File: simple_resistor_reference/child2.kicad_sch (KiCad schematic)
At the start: 1 part

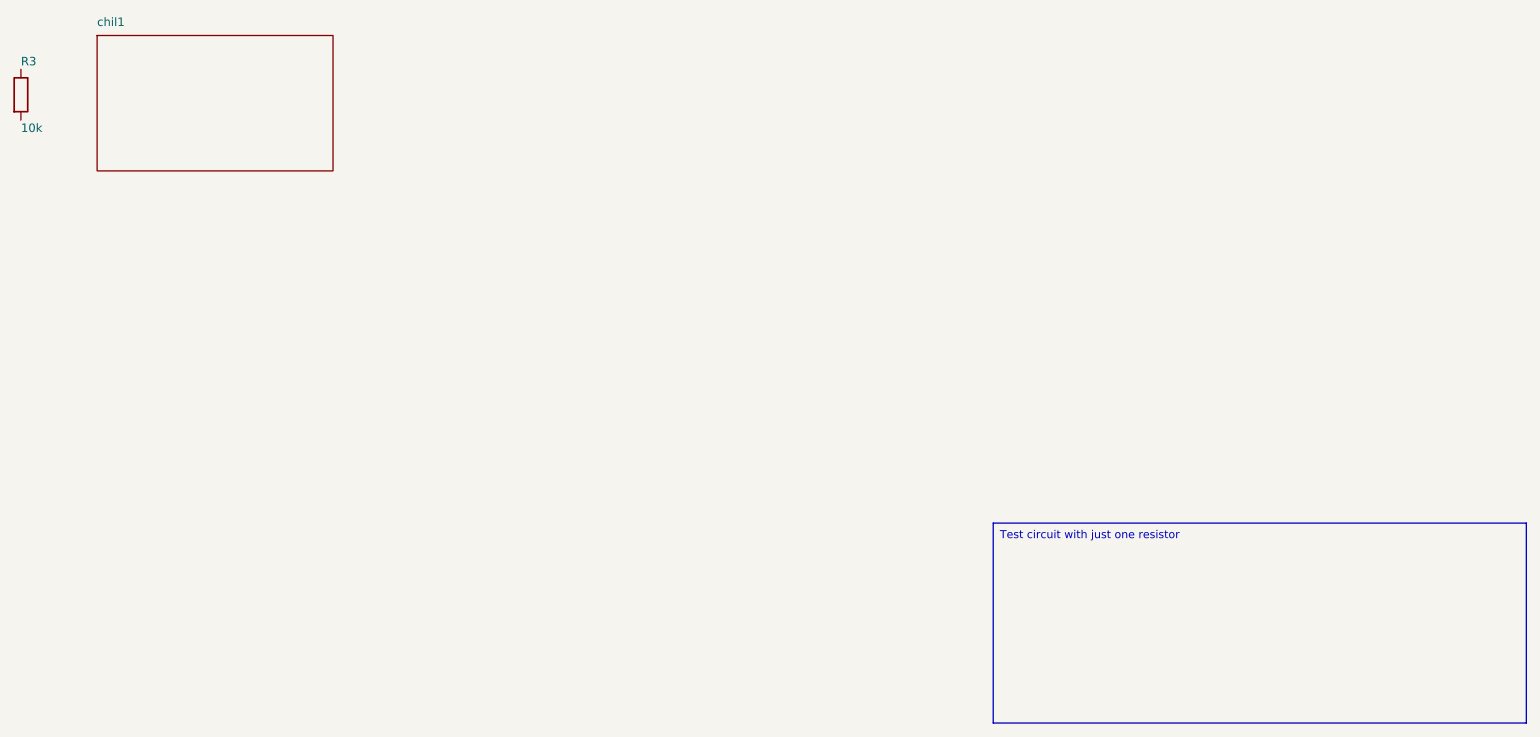
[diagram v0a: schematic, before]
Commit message: adding updated testing code
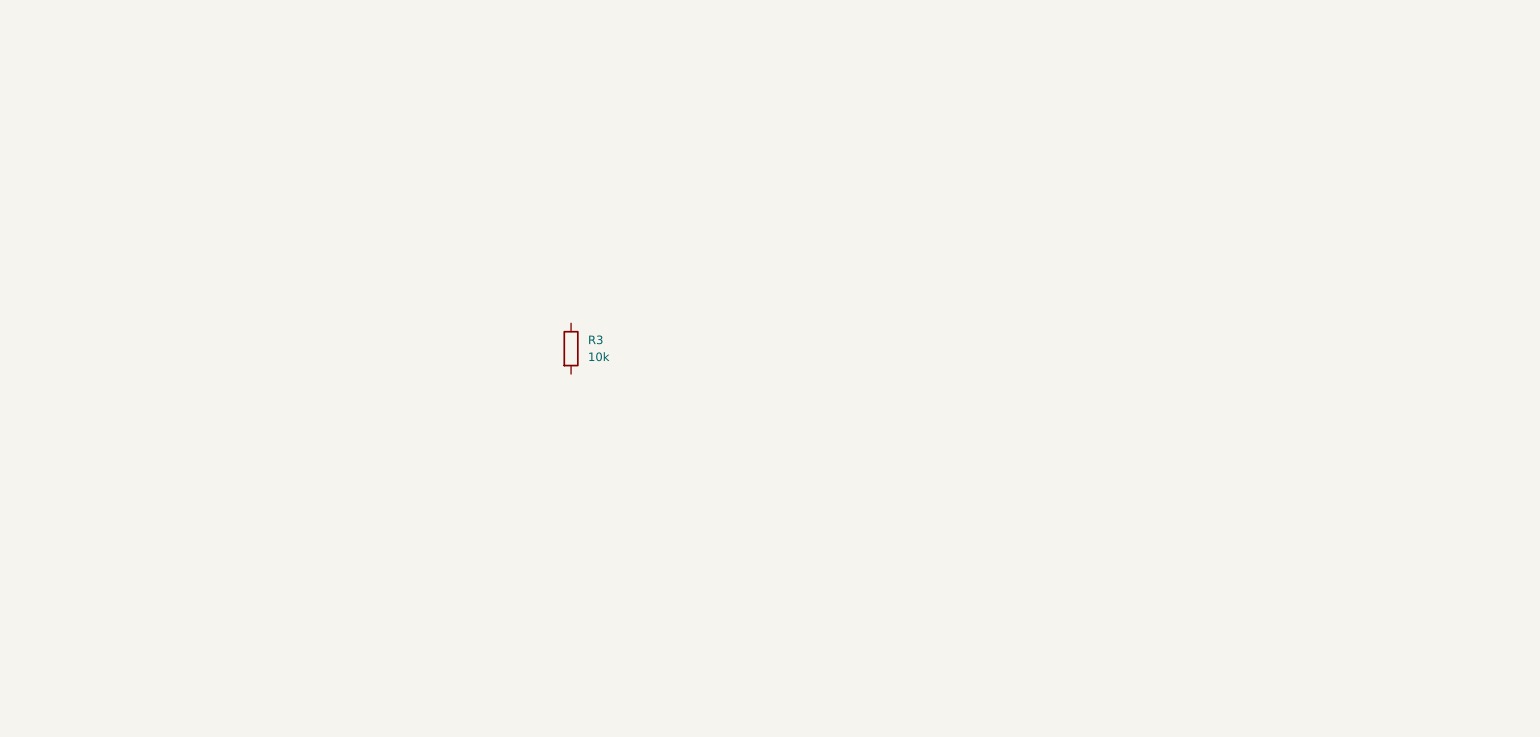
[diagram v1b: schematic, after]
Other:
- removed sheet chil1
- company: Circuit-Synth -> (none)
- title: singe_resistor_generated -> (none)
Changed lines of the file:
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@@
 (kicad_sch
 	(version 20250114)
-	(generator "kicad_api")
+	(generator "eeschema")
 	(generator_version "9.0")
 	(paper "A4")
-	(title_block
-		(title singe_resistor_generated)
-		(date 2025-08-04)
-		(company Circuit-Synth)
-	)
 	(symbol
 		(lib_id "Device:R")
-		(at 38.1 45.72 0)
+		(at 120.65 83.82 0)
 		(unit 1)
 		(exclude_from_sim no)
@@
 		(fields_autoplaced yes)
 		(property "Reference" "R3"
-			(at 38.1 40.72 0)
+			(at 123.19 82.5499 0)
 			(effects
 				(font
@@
 		)
 		(property "Value" "10k"
-			(at 38.1 50.72 0)
+			(at 123.19 85.0899 0)
 			(effects
 				(font
@@
 		)
 		(property "Footprint" "Resistor_SMD:R_0603_1608Metric"
-			(at 38.1 55.72 0)
+			(at 118.872 83.82 90)
 			(effects
 				(font
@@
 			)
 		)
+		(property "Datasheet" "~"
+			(at 120.65 83.82 0)
+			(effects
+				(font
+					(size 1.27 1.27)
+				)
+				(hide yes)
+			)
+		)
+		(property "Description" "Resistor"
+			(at 120.65 83.82 0)
+			(effects
+				(font
+					(size 1.27 1.27)
+				)
+				(hide yes)
+			)
+		)
+		(pin "2"
+		)
+		(pin "1"
+		)
 		(instances
-			(project
-				""
-				(path
-					"/4230698c-b526-4307-9655-afb80e239726"
+			(project "simple_resistor_reference"
+				(path "/8ea40386-79fd-4dea-8cc4-e20a6a247364/5c9a6dd5-fe4a-4d9b-993b-8c5ee2461010/db6c7bdb-be8f-47ca-ac20-40a64e7f00e4"
 					(reference "R3")
 					(unit 1)
@@
 		)
 	)
-	(sheet
-		(at 49.53 36.83)
-		(size 35.4 20.32)
-		(stroke
-			(width 0.12)
-			(type solid)
-		)
-		(fill
-			(color
-				0
-				0
-				0
-				0.0
-			)
-		)
-		(property "Sheetname" "chil1"
-			(at 49.53 35.559999999999995 0)
-			(effects
-				(font
-					(size 1.27 1.27)
-				)
-				(justify left bottom)
-			)
-		)
-		(property "Sheetfile" "chil1.kicad_sch"
-			(at 49.53 58.42 0)
-			(effects
-				(font
-					(size 1.27 1.27)
-				)
-				(justify left top)
-				(hide yes)
-			)
-		)
-		(instances
-			(project
-				"single_resistor_generated"
-				(path
-					"/"
-					(page "1")
-				)
-			)
-		)
-	)
-	(text_box
-		"Test circuit with just one resistor"
-		(exclude_from_sim yes)
-		(at 184.0 110.0 0)
-		(size 80.0 30.0)
-		(margins
-			1.0
-			1.0
-			1.0
-			1.0
-		)
-		(stroke
-			(width 0.1)
-			(type solid)
-		)
-		(fill
-			(type color)
-			(color
-				255
-				255
-				224
-				1
-			)
-		)
-		(effects
-			(font
-				(size 1.2 1.2)
-				(thickness 0.254)
-			)
-			(justify left top)
-		)
-	)
-	(sheet_instances
-		(path
-			"/4230698c-b526-4307-9655-afb80e239726"
-			(page "1")
-		)
-	)
-	(embedded_fonts no)
 )
